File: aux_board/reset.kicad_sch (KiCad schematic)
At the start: 2 parts, among them SW1 EVP-AA602W

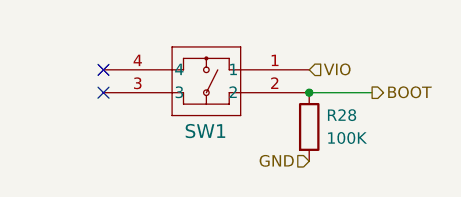
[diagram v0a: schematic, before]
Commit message: tweaking SCI and AUX for production, using common sheets as much as possible
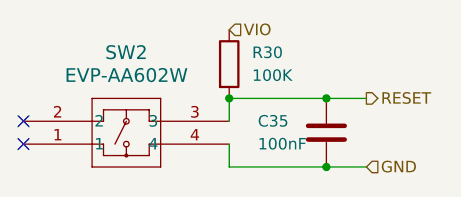
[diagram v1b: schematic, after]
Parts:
- removed R28: 100K, Resistor_SMD:R_0402_1005Metric_Pad0.72x0.64mm_HandSolder, symbol Device:R
- removed SW1: EVP-AA602W, Project:EVP602AA, symbol Project:EVP-AA602W
- added C35: 100nF, Capacitor_SMD:C_0402_1005Metric_Pad0.74x0.62mm_HandSolder, symbol Device:C
- added R30: 100K, Resistor_SMD:R_0402_1005Metric_Pad0.72x0.64mm_HandSolder, symbol Device:R
- added SW2: EVP-AA602W, Project:EVP602AA, symbol Project:EVP-AA602W
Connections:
- net GND: now also C35.2, SW2.4
- net VIO: now also R30.1
- new net RESET: C35.1, R30.2, SW2.3
